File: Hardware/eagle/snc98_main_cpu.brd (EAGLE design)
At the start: 168.1 x 54.1 mm, 151 parts, among them IC1 MCP170333MB, M1 IRLML2244, M10 IRLML2244, M11 IRLML2244, M12 IRLML2244, M2 IRLML2244, M3 IRLML2244, M4 IRLML2244, M5 IRLML2244, M6 IRLML2244, M7 IRLML2244, M8 IRLML2244, M9 IRLML2244, U1 74HC4051_MUX, U3 ATMEGA1284P-PU, U4 TLV70033, X1 MICROMATCH-12, X3 MICROMATCH-12, Y2 12MHz

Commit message: snc98_main_cpu V1.0
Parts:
- removed BH4, BH5: HOLDER_AAA_LEFT1, SparkFun-Electromechanical:BATTERY-AAA-LEFT
- removed BH6: HOLDER_AAA_RIGHT, SparkFun-Electromechanical:BATTERY-AAA-RIGHT
- removed D14, D15, D16, D17, D18, D19, D2, D20, D21, D22, D23, D24, D25, D26, D27: SC40-11_UNISC40-11_UNI, display-hp:10MM_UNI
- removed JP1, JP4: RXD_1, adafruit:1X01-CLEANBIG
- removed JP10, JP11, JP12, JP7, JP8, JP9: (no value), adafruit:1X01
- removed JP2: TXD_1, adafruit:1X01-CLEANBIG
- removed KP1, KP2: KEYPAD, KeyPad3x4:KEYPAD
- removed M10, M11, M4, M5, M6, M7, M8, M9: IRLML2244, IRLML6402:SOT-23
- removed R10, R11, R12, R13, R14, R15, R16, R17, R18, R19, R5, R6, R7, R8, R9: 22, rcl:R1210
- removed R26: 6k8, rcl:0204/5
- removed R29, R54, R55, R56, R57, R58, R59: 3k3, rcl:0204/5
- removed R30: 3V3, rcl:0204/5
- removed R36, R37, R38, R39, R40, R41, R42, R43: 3k3, rcl:R1206
- removed X1, X3: MICROMATCH-12, Con-amp-micromatch:MICROMATCH-12
- added C13: 100n, rcl:C1206K
- added JP15: (no value), adafruit:1X09-BIG
- added JP3: (no value), adafruit:1X08-CLEANBIG
- C1, C2, C3, C6: device _jc:C025_050-025X075 -> _jc:C1206K
- C14, C15, C18, C4, C9: device rcl:C025_050-025X075 -> rcl:C1206K
- C7, C8: device _jc:C025-024X044 -> _jc:C0805K
- LOGO2: value OSHW_LOGO_6MILX0100-NT -> OSHW_LOGO_8MILX0150-NT; device ohw-logo:OSHW_6X100_NOTEXT -> ohw-logo:OSHW_8X150_NOTEXT
- R1, R21, R22, R25, R28, R31, R32, R33, R34, R35, R4, R44, R46, R47, R48, R50, R51: device rcl:0204/7 -> rcl:R1206
- R2: value 6k8 -> 56R
- R20: device rcl:0204/5 -> rcl:R1206
- U$2: device transistor-power:MICRO3 -> transistor-power:SOT-23
- U$3: value HT7333 -> HT7333 / TS9011SCY
- U4: value TLV70033 -> TLV70033 / TC1185
- moved S3 217.4 mm to (152.5, 11.3)
- moved R3 194.3 mm to (138.2, 9.65), flipped to the bottom
- moved R23 179.0 mm to (122.9, 6.60), flipped to the bottom, turned to 270 degrees
- moved D1 171.7 mm to (100.1, 10.2), flipped to the bottom, turned to 90 degrees
- moved U4 170.9 mm to (106.7, 12.2), flipped to the bottom
- moved R25 169.2 mm to (141.2, 7.11), flipped to the bottom, turned to 180 degrees
- moved C5 168.7 mm to (138.2, 12.2), flipped to the bottom
- moved C12 161.6 mm to (126.0, 1.02), flipped to the bottom, turned to 180 degrees
- moved C20 161.1 mm to (90.2, 12.4), flipped to the bottom, turned to 0 degrees
- moved C11 160.7 mm to (109.9, 11.8), flipped to the bottom, turned to 90 degrees
- moved C10 160.4 mm to (125.5, 6.60), flipped to the bottom, turned to 90 degrees
- moved C21 159.1 mm to (95.9, 12.2), flipped to the bottom, turned to 0 degrees
- moved R27 158.2 mm to (120.8, 6.60), flipped to the bottom, turned to 270 degrees
- moved D8 150.1 mm to (80.0, 4.32), flipped to the bottom
- moved U$2 149.4 mm to (117.0, 6.99), flipped to the bottom, turned to 180 degrees
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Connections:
- removed net CA_LED: M10.2, M11.2, M4.2, M5.2, M6.2, M7.2, M8.2, M9.2, R29.1, R30.1, R36.1, R37.1, R38.1, R39.1, R40.1, R41.1, R42.1, R43.1, R54.1, R55.1, R56.1, R57.1, R58.1, R59.1, X3.8
- removed net D0_A: R5.2, X3.1
- removed net D10_A: R15.2, X1.8
- removed net D11_A: R16.2, X1.9
- removed net D12_A: R17.2, X1.10
- removed net D13_A: R18.2, X1.11
- removed net D14_A: R19.2, X1.12
- removed net D1_A: R6.2, X3.2
- removed net D2_A: R7.2, X3.3
- removed net D3_A: R8.2, X3.4
- removed net D4_A: R9.2, X3.5
- removed net D5_A: R10.2, X3.6
- removed net D6_A: R11.2, X3.7
- removed net D7_A: R12.2, X1.5
- removed net D8_A: R13.2, X1.6
- removed net D9_A: R14.2, X1.7
- removed net DIG_0: D2.11, D2.12, D2.13, D2.14, D2.23, D2.28, R5.1
- removed net DIG_1: D14.11, D14.12, D14.13, D14.14, D14.23, D14.28, R6.1
- removed net DIG_10: D23.11, D23.12, D23.13, D23.14, D23.23, D23.28, R15.1
- removed net DIG_11: D24.11, D24.12, D24.13, D24.14, D24.23, D24.28, R16.1
- removed net DIG_12: D25.11, D25.12, D25.13, D25.14, D25.23, D25.28, R17.1
- removed net DIG_13: D26.11, D26.12, D26.13, D26.14, D26.23, D26.28, R18.1
- removed net DIG_14: D27.11, D27.12, D27.13, D27.14, D27.23, D27.28, R19.1
- removed net DIG_2: D15.11, D15.12, D15.13, D15.14, D15.23, D15.28, R7.1
- removed net DIG_3: D16.11, D16.12, D16.13, D16.14, D16.23, D16.28, R8.1
- removed net DIG_4: D17.11, D17.12, D17.13, D17.14, D17.23, D17.28, R9.1
- removed net DIG_5: D18.11, D18.12, D18.13, D18.14, D18.23, D18.28, R10.1
- removed net DIG_6: D19.11, D19.12, D19.13, D19.14, D19.23, D19.28, R11.1
- removed net DIG_7: D20.11, D20.12, D20.13, D20.14, D20.23, D20.28, R12.1
- removed net DIG_8: D21.11, D21.12, D21.13, D21.14, D21.23, D21.28, R13.1
- removed net DIG_9: D22.11, D22.12, D22.13, D22.14, D22.23, D22.28, R14.1
- removed net GND1: C22.2
- removed net IO-A: M4.1, R29.2, R36.2, X1.4
- removed net IO-B: M5.1, R30.2, R37.2, X1.3
- removed net IO-C: M6.1, R42.2, R54.2, X1.2
- removed net IO-D: M7.1, R38.2, R55.2, X1.1
- removed net IO-DP: M11.1, R41.2, R59.2, X3.9
- removed net IO-E: M8.1, R43.2, R56.2, X3.12
- removed net IO-F: M9.1, R39.2, R57.2, X3.11
- removed net IO-G: M10.1, R40.2, R58.2, X3.10
- removed net N$2: U$2.2
- removed net NC1: BH4.P1, BH4.P2, BH4.P3, BH4.P4, BH7.P1, BH7.P2, BH7.P3, BH7.P4
- removed net NC2: BH5.P1, BH5.P2, BH5.P3, BH5.P4
- removed net NC3: BH6.M1, BH6.M2, BH6.M3, BH6.M4
- removed net SEG_A: D14.10, D14.27, D15.10, D15.27, D16.10, D16.27, D17.10, D17.27, D18.10, D18.27, D19.10, D19.27, D2.10, D2.27, D20.10, D20.27, D21.10, D21.27, D22.10, D22.27, D23.10, D23.27, D24.10, D24.27, D25.10, D25.27, D26.10, D26.27, D27.10, D27.27, M4.3
- removed net SEG_B: D14.26, D14.9, D15.26, D15.9, D16.26, D16.9, D17.26, D17.9, D18.26, D18.9, D19.26, D19.9, D2.26, D2.9, D20.26, D20.9, D21.26, D21.9, D22.26, D22.9, D23.26, D23.9, D24.26, D24.9, D25.26, D25.9, D26.26, D26.9, D27.26, D27.9, M5.3
- removed net SEG_C: D14.24, D14.7, D15.24, D15.7, D16.24, D16.7, D17.24, D17.7, D18.24, D18.7, D19.24, D19.7, D2.24, D2.7, D20.24, D20.7, D21.24, D21.7, D22.24, D22.7, D23.24, D23.7, D24.24, D24.7, D25.24, D25.7, D26.24, D26.7, D27.24, D27.7, JP10.1, JP11.1, JP8.1, M6.3
- removed net SEG_D: D14.22, D14.5, D15.22, D15.5, D16.22, D16.5, D17.22, D17.5, D18.22, D18.5, D19.22, D19.5, D2.22, D2.5, D20.22, D20.5, D21.22, D21.5, D22.22, D22.5, D23.22, D23.5, D24.22, D24.5, D25.22, D25.5, D26.22, D26.5, D27.22, D27.5, M7.3
- removed net SEG_DP: D14.25, D14.6, D14.8, D15.25, D15.6, D15.8, D16.25, D16.6, D16.8, D17.25, D17.6, D17.8, D18.25, D18.6, D18.8, D19.25, D19.6, D19.8, D2.25, D2.6, D2.8, D20.25, D20.6, D20.8, D21.25, D21.6, D21.8, D22.25, D22.6, D22.8, D23.25, D23.6, D23.8, D24.25, D24.6, D24.8, D25.25, D25.6, D25.8, D26.25, D26.6, D26.8, D27.25, D27.6, D27.8, JP12.1, JP7.1, JP9.1, M11.3
- removed net SEG_E: D14.21, D14.4, D15.21, D15.4, D16.21, D16.4, D17.21, D17.4, D18.21, D18.4, D19.21, D19.4, D2.21, D2.4, D20.21, D20.4, D21.21, D21.4, D22.21, D22.4, D23.21, D23.4, D24.21, D24.4, D25.21, D25.4, D26.21, D26.4, D27.21, D27.4, M8.3
- removed net SEG_F: D14.2, D14.29, D15.2, D15.29, D16.2, D16.29, D17.2, D17.29, D18.2, D18.29, D19.2, D19.29, D2.2, D2.29, D20.2, D20.29, D21.2, D21.29, D22.2, D22.29, D23.2, D23.29, D24.2, D24.29, D25.2, D25.29, D26.2, D26.29, D27.2, D27.29, M9.3
- removed net SEG_G: D14.1, D14.3, D14.30, D15.1, D15.3, D15.30, D16.1, D16.3, D16.30, D17.1, D17.3, D17.30, D18.1, D18.3, D18.30, D19.1, D19.3, D19.30, D2.1, D2.3, D2.30, D20.1, D20.3, D20.30, D21.1, D21.3, D21.30, D22.1, D22.3, D22.30, D23.1, D23.3, D23.30, D24.1, D24.3, D24.30, D25.1, D25.3, D25.30, D26.1, D26.3, D26.30, D27.1, D27.3, D27.30, M10.3
- net A4: no longer JP4.1
- net A5: now also JP15.8, JP3.8; no longer KP1.C_2, KP2.C_2
- net A6: now also JP15.7, JP3.7; no longer KP1.C_1, KP2.C_1
- net A7: now also JP15.6, JP3.6; no longer KP1.C_0, KP2.C_0
- net A9: no longer R26.2
- net AREF: now also JP15.9
- net D10_: no longer JP1.1
- net D11_: no longer JP2.1
- net EN: no longer R2.2, R26.1
- net GND: now also U$2.2; no longer R2.1, S3.P$15
- net GND-ISO: now also C13.1, JP15.1, JP3.1
- net IO_A: now also JP15.5; no longer KP2.R_0
- net IO_B: now also JP15.4; no longer KP2.R_1
- net IO_C: now also JP15.3; no longer KP2.R_2
- net IO_D: now also JP15.2; no longer KP2.R_3
- net IO_DP: now also JP3.2; no longer KP1.R_3
- net IO_E: now also JP3.5; no longer KP1.R_0
- net IO_F: now also JP3.4; no longer KP1.R_1
- net IO_G: now also JP3.3; no longer KP1.R_2
- net N$1: now also C22.2
- net N$13: now also R2.2
- net N$6: now also R25.2
- net VIN_P: now also R2.1
- net V_IN: now also BH7.P1, BH7.P2, BH7.P3, BH7.P4, C13.2, S3.P$15, U$3.VIN
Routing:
- net SEG_DP: track 347.3 -> 0.00 mm
- net SEG_G: track 337.5 -> 0.00 mm
- net SEG_A: track 335.2 -> 0.00 mm
- net SEG_F: track 306.0 -> 0.00 mm, vias 32 -> 0
- net GND-ISO: track 0.00 -> 303.4 mm, vias 0 -> 15
- net SEG_C: track 281.2 -> 0.00 mm, vias 29 -> 0
- net SEG_B: track 267.0 -> 0.00 mm, vias 15 -> 0
- net V_IN: track 0.00 -> 266.2 mm, vias 0 -> 8
- net SEG_E: track 254.6 -> 0.00 mm, vias 1 -> 0
- net VCC: track 0.00 -> 213.3 mm, vias 0 -> 10
- net SEG_D: track 209.0 -> 0.00 mm, vias 16 -> 0
- net GND: track 0.00 -> 179.5 mm, vias 6 -> 8
- net CA_LED: track 163.1 -> 0.00 mm, vias 4 -> 0
- net N$23: track 0.00 -> 132.4 mm, vias 0 -> 3
- net CA_PWM: track 0.00 -> 108.8 mm, vias 0 -> 3
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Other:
- board size 168.1 x 54.1 mm -> 168.1 x 32.8 mm
- board text added: "CUT OUT"
- board text added: "https://oshpark. com/profiles/Jens_G"
- board text added: "https://oshpark.com/ profiles/Jens_G"
- board text removed: "RESET"
- board text removed: "https://oshpark.com/profiles/Jens_G"

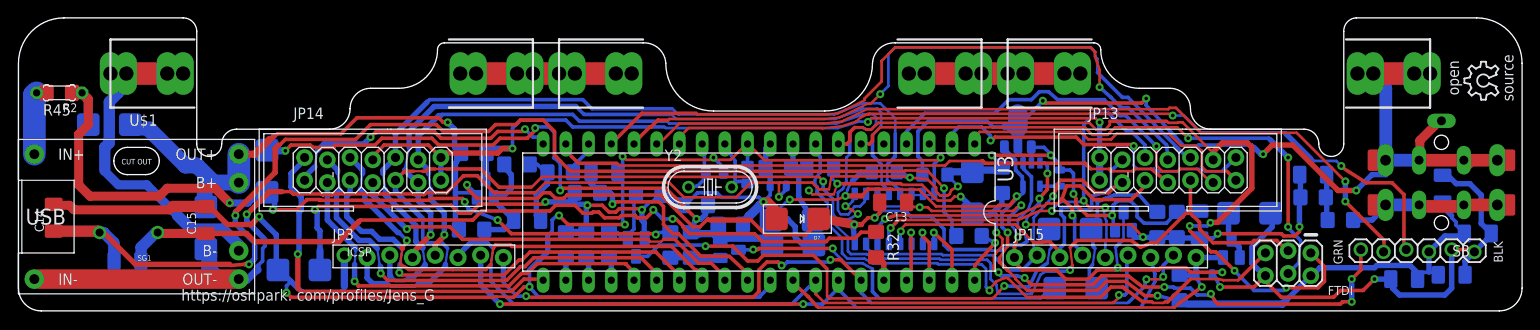
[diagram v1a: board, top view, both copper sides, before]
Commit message: new Reset on Main:cpu
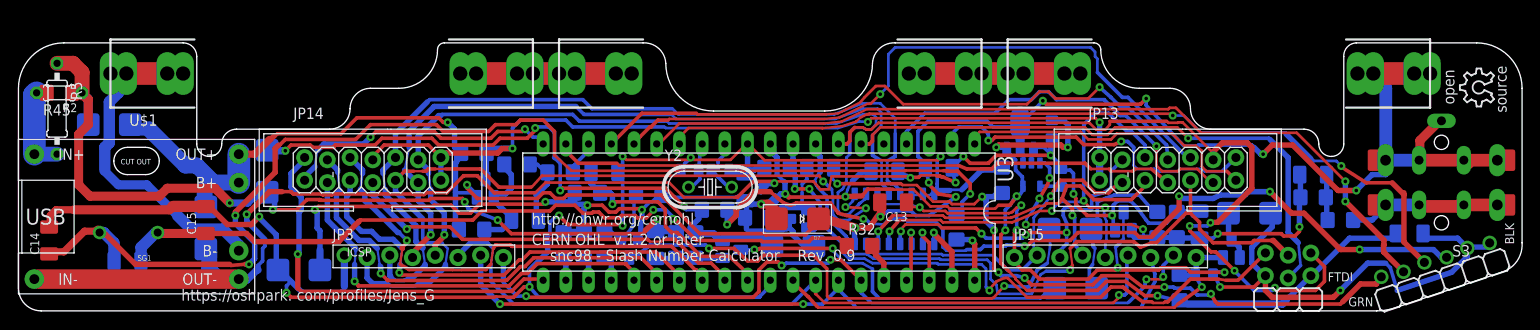
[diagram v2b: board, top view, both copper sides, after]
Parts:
- removed D1, D6: SD103CW, BaseApp:SMADIODE
- removed R24: 2R7, rcl:R1206
- added R5: 56R, rcl:0207/10
- added R6: 22k, rcl:R1206
- added T1: BCR135, digital-transistors:SOT23-BEC
- C3: value 100nF -> 0.1uF; device _jc:C1206K -> SparkFun:0805
- C6: value 10uF -> 15n; device _jc:C1206K -> rcl:C1206K
- R1, R44, R47: value 47k -> 22k
- R20: value 2R7 -> 1k
- R25: value 100 -> 1k
- R31, R32: value 100 -> 150
- R33: value 1k -> 6k8
- SG1: value BUZZERNS -> SBT1205-3
- moved C6 89.1 mm to (64.6, 4.32), turned to 90 degrees
- moved C1 74.4 mm to (74.7, 10.8), turned to 90 degrees
- moved C3 44.2 mm to (109.0, 17.3), turned to 270 degrees
- moved JP6 10.8 mm to (145.8, 0.76), turned to 18.5 degrees
- moved C2 7.62 mm to (149.0, 5.61)
- moved R1 6.04 mm to (76.1, 7.37)
- moved JP5 5.80 mm to (132.8, 0.76), turned to 0 degrees
- moved C7 3.09 mm to (71.9, 12.7), turned to 180 degrees
- moved C8 2.81 mm to (68.5, 12.7), turned to 0 degrees
- moved C14 2.59 mm to (-3.17, 4.83)
- moved R20 2.22 mm to (71.2, 8.26), turned to 180 degrees
- moved R32 1.86 mm to (87.5, 4.22), turned to 0 degrees
- moved R31 1.73 mm to (98.3, 6.35), turned to 90 degrees
- moved C16 1.45 mm to (77.2, 10.0), turned to 45 degrees
- moved LOGO2 0.92 mm to (158.4, 19.8)
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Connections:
- removed net N$12: C18.2, D1.C, JP6.6, R51.2
- new net DTR: C18.2, JP6.1, R51.2
- new net R_: C18.1, R1.2, T1.B
- new net VCC_IN: JP6.4, R20.2
- net /RESET: now also JP5.2, R6.1, T1.E; no longer C18.1, D6.A, JP5.5, R1.2
- net AREF: now also C12.3; no longer C12.1
- net D5_: now also JP5.3; no longer JP5.4
- net D6_: now also JP5.6; no longer JP5.1
- net D7_: now also JP5.4; no longer JP5.3
- net D8_: now also JP6.3; no longer JP6.4
- net D9_: now also JP6.2; no longer JP6.5
- net GND: now also C11.4, C16.4, C3.4; no longer C11.2, C16.2, D1.A, R51.1
- net GND-ISO: now also C12.4, JP5.1, JP6.5, JP6.6, R51.1, R6.2; no longer C12.2, C3.2, C6.2, JP5.6, JP6.1, JP6.2
- net N$13: now also R5.2
- net N$3: now also C11.3; no longer C11.1
- net N$9: now also C6.1
- net VCC: now also C16.3, C3.3, JP5.5, T1.C; no longer C16.1, C3.1, C6.1, D6.C, JP5.2, JP6.3, R20.2, R24.2
- net VIN_P: now also C6.2, R5.1
- net XX_3: no longer R24.1
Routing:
- net VCC_IN: track 0.00 -> 96.0 mm, vias 0 -> 6
- net N$12: track 85.3 -> 0.00 mm, vias 10 -> 0
- net DTR: track 0.00 -> 77.8 mm, vias 0 -> 7
- net V_IN: track 266.2 -> 249.9 mm, vias 8 -> 10
- net R_: track 0.00 -> 9.83 mm
- net VIN_P: track 89.8 -> 97.8 mm
- net GND-ISO: track 303.4 -> 310.3 mm
- net D11_: track 75.8 -> 71.2 mm
- net XX_3: track 77.4 -> 73.5 mm
- net VCC: track 213.3 -> 209.9 mm, vias 10 -> 12
- net N$10: track 90.1 -> 86.9 mm
- net D9_: track 91.5 -> 94.7 mm
- net N$9: track 5.59 -> 8.49 mm
- net D8_: track 92.5 -> 95.1 mm
- net N$13: track 9.24 -> 11.8 mm
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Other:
- board size 168.1 x 32.8 mm -> 168.2 x 30 mm
- board text added: "snc98 - Slash Number Calculator Rev. 0.9"
- board text removed: "snc98 - Slash Number Calculator Rev. 0.8"

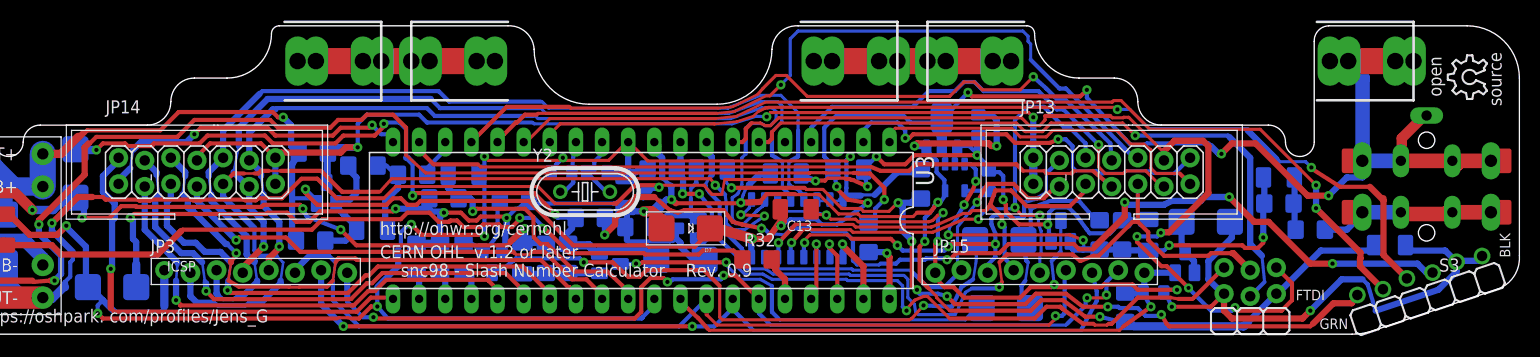
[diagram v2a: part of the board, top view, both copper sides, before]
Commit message: Main_cpu_rev_0.95 - Add Onewire DS18B20
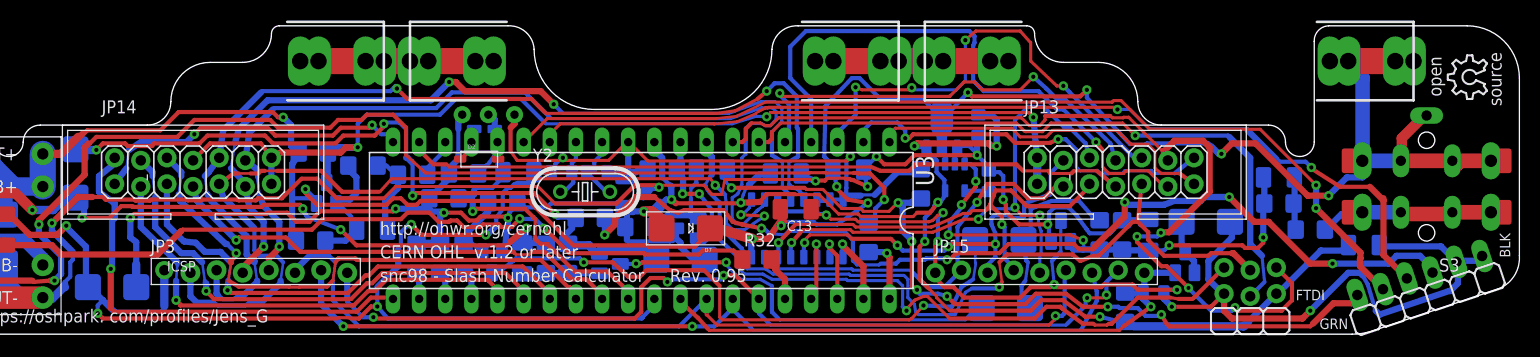
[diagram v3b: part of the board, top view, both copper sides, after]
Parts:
- added D1: SD103CW, BaseApp:SOD-323
- added D2: SD103CW, BaseApp:SOD-123
- added R7: 6k8, rcl:R1206
- added U2: DS18B20, SparkFun-Sensors:TO-92-AMMO
- moved C4 5.34 mm to (64.3, 12.7)
- moved C2 2.54 mm to (146.4, 5.61)
- moved R28 1.15 mm to (62.7, 9.78)
- moved JP13 0.38 mm to (122.3, 12.7)
- moved JP14 0.38 mm to (32.6, 12.7)
- moved BH9 0.25 mm to (108.1, 23.5)
- moved BH10 0.25 mm to (46.9, 23.5)
- moved BH11 0.13 mm to (96.9, 23.5)
- moved BH12 0.13 mm to (58.0, 23.5)
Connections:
- net D8_ renamed D8_RX0
- net D9_ renamed D9_TX0
- removed net D10_: JP13.10, U3.16
- removed net D11_: JP13.8, U3.17
- new net D10_RX1: D1.A, D2.A, R7.1, U2.2, U3.16
- new net D11_TX1: D1.C, D2.C, U3.17
- net D2_: now also JP13.10
- net D4_: now also JP13.8
- net GND-ISO: now also U2.1
- net VCC: now also R7.2, U2.3
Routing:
- net D10_: track 75.5 -> 0.00 mm, vias 1 -> 0
- net D11_: track 71.2 -> 0.00 mm, vias 1 -> 0
- net D2_: track 0.00 -> 45.8 mm, vias 0 -> 4
- net D4_: track 0.00 -> 43.3 mm, vias 0 -> 2
- net D3_: track 43.2 -> 57.5 mm
- net VCC: track 209.9 -> 219.2 mm
- net D10_RX1: track 0.00 -> 8.87 mm
- net GND-ISO: track 310.3 -> 318.6 mm, vias 15 -> 14
- net V_IN: track 249.9 -> 253.6 mm
- net D11_TX1: track 0.00 -> 3.53 mm
- net IO_G: track 93.3 -> 96.2 mm, vias 0 -> 2
- net N$8: track 9.90 -> 7.50 mm
- net AVCC: track 25.7 -> 27.6 mm
- net CA_PWM: track 108.8 -> 110.5 mm
- net N$1: track 14.5 -> 12.8 mm
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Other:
- outline, holes or cut-outs redrawn
- board text added: "snc98 - Slash Number Calculator Rev. 0.95"
- board text removed: "snc98 - Slash Number Calculator Rev. 0.9"

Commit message: fine with 2 numbers
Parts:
- C1: value 100nF -> 220nF
- C12: value 0.1uF -> 47n
- C13, C5: value 100n -> 47n
- C16, C3: value 0.1uF -> 220nF
- C18: value 100n -> 220n
- moved Y2 1.49 mm to (69.3, 10.3)
- moved SG1 1.14 mm to (4.70, 5.21)
- moved C9 1.02 mm to (4.57, 2.54)
- moved R51 0.38 mm to (103.0, 11.6)
- moved D7 0.25 mm to (80.8, 7.24)
- moved R20 0.25 mm to (71.0, 8.26)
- moved R4 0.25 mm to (56.8, 10.2)
- moved D1 0.25 mm to (61.0, 16.6)
- moved R28 0.25 mm to (62.5, 9.78)
- moved R50 0.25 mm to (123.0, -0.43)
- moved C7 0.13 mm to (71.8, 12.7)
- moved C8 0.13 mm to (68.3, 12.7)
- moved U4 0.13 mm to (106.7, 12.1)
- moved M12 0.13 mm to (73.2, 3.68)
- moved C1 0.13 mm to (74.5, 10.8)
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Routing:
- net VIN_P: track 98.0 -> 92.7 mm
- net VCC: track 219.2 -> 224.0 mm
- net D10_RX1: track 8.87 -> 10.9 mm
- net GND-ISO: track 318.6 -> 320.2 mm
- net N$10: track 86.7 -> 87.8 mm
- net XTAL1: track 5.81 -> 6.90 mm
- net GND: track 177.8 -> 178.5 mm
- net N$23: track 133.2 -> 132.6 mm
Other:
- outline, holes or cut-outs redrawn

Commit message: Add new Function: mod (modular)
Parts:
- added T2: BCR135, digital-transistors:SOT23-BEC
- added T3: BCR185, digital-transistors-1(1):SOT23-R_INFINEON
- R2, R45, R5: value 56R -> 150R
- moved T1 3.02 mm to (77.7, 8.00), turned to 180 degrees
- moved C16 2.81 mm to (74.5, 10.9), turned to 0 degrees
- moved C1 2.51 mm to (73.3, 13.0), turned to 0 degrees
- moved C7 2.50 mm to (69.5, 11.7), turned to 90 degrees
- moved R1 1.33 mm to (74.8, 7.75), turned to 90 degrees
- moved S3 0.80 mm to (152.8, 12.1)
- moved IC1 0.74 mm to (106.0, 17.4)
- moved C8 0.74 mm to (67.7, 12.3), turned to 90 degrees
- moved U$3 0.65 mm to (106.0, 16.0)
- moved C11 0.38 mm to (110.4, 11.8)
- moved C3 0.38 mm to (109.3, 17.3)
- moved U4 0.38 mm to (107.1, 12.1)
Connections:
- removed net AREF: C12.3, JP15.9, M1.2, R50.1, U3.32
- new net AREF_+1V: C12.3, JP15.9, M1.2, R50.1, T3.B, U3.32
- new net N$2: T1.E, T3.E
- net /RESET: now also T3.C; no longer T1.E
- net VCC: now also T2.E
- net V_IN: now also T2.B, T2.C
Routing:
- net AREF_+1V: track 0.00 -> 63.8 mm, vias 0 -> 1
- net AREF: track 57.1 -> 0.00 mm, vias 1 -> 0
- net VCC: track 224.0 -> 234.1 mm, vias 12 -> 13
- net V_IN: track 253.7 -> 262.2 mm
- net N$6: track 19.5 -> 24.0 mm
- net XTAL2: track 6.89 -> 9.39 mm
- net N$2: track 0.00 -> 2.13 mm
- net XTAL1: track 6.90 -> 8.75 mm
- net VCC_IN: track 96.7 -> 95.4 mm
- net GND: track 178.5 -> 179.6 mm
- net N$9: track 8.49 -> 7.94 mm
- net /RESET: track 72.7 -> 72.2 mm
- net R_: track 9.83 -> 10.3 mm
- net GND-ISO: track 320.2 -> 319.7 mm, vias 14 -> 15

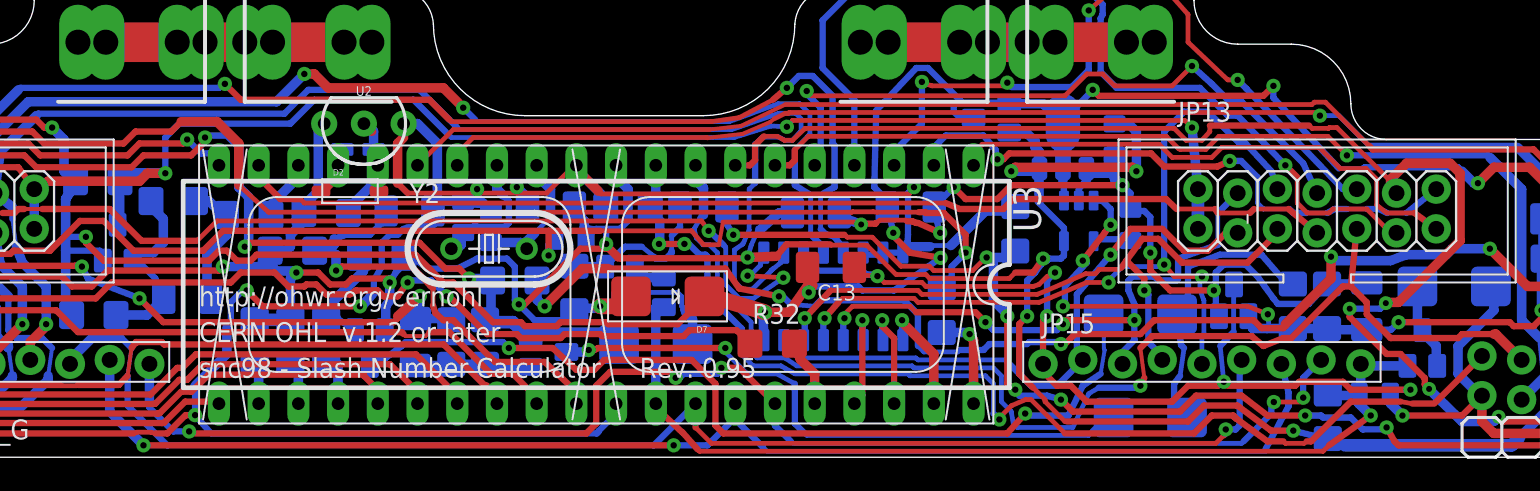
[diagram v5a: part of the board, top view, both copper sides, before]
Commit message: Work like WIN_7 Calculator in "Standard Mode"
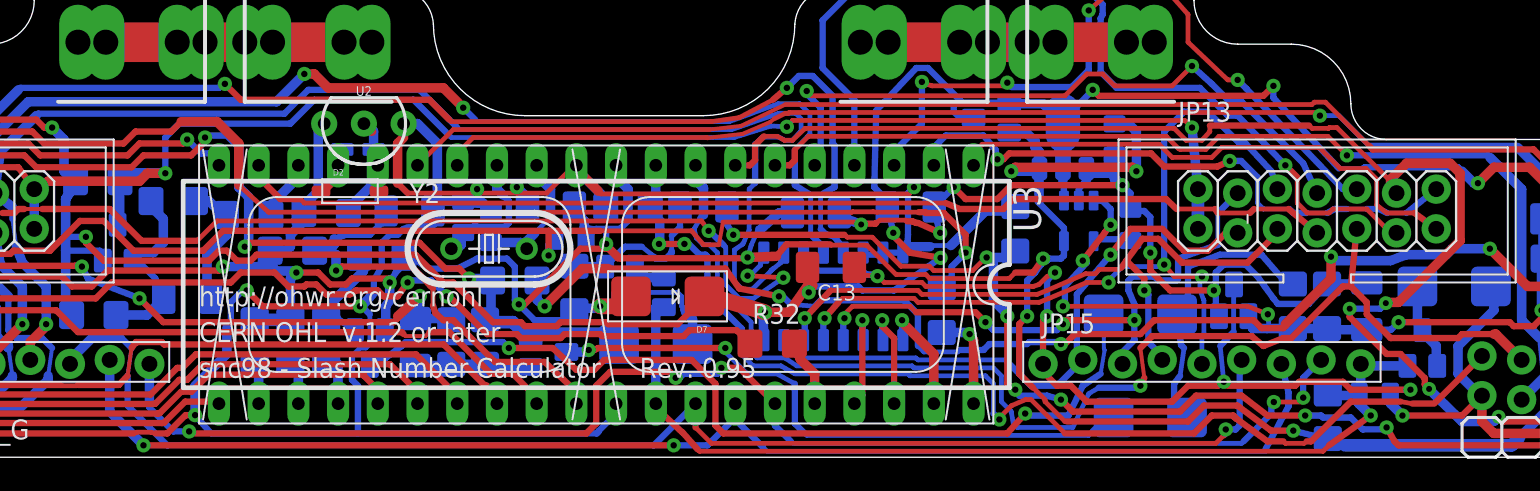
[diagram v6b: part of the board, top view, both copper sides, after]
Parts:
- R1: value 22k -> 47k
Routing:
- net GND-ISO: track 319.7 -> 328.9 mm

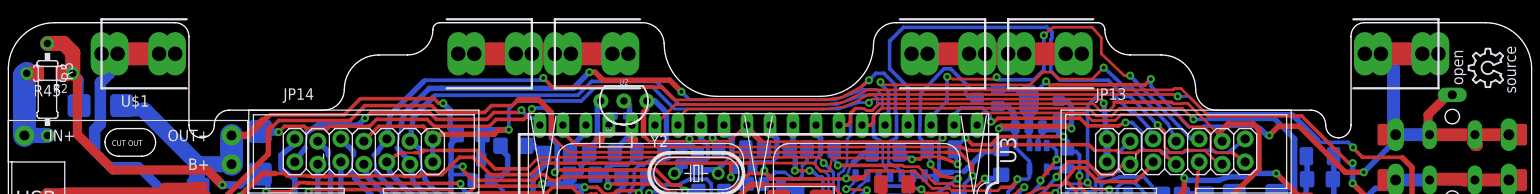
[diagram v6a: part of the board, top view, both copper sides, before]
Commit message: Version 4 mechanical change
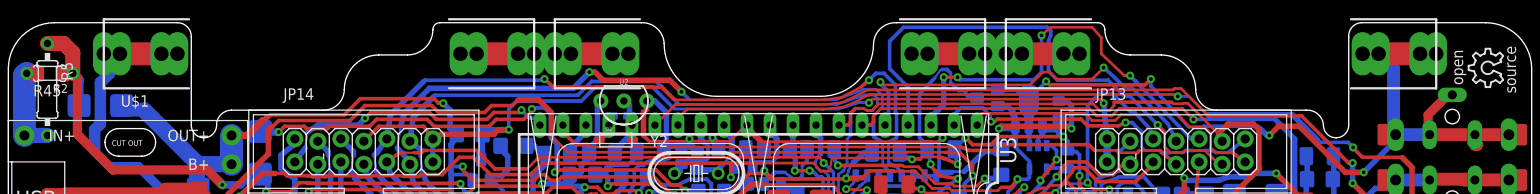
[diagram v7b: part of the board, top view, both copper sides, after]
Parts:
- moved BH9 0.25 mm to (107.8, 23.5)
- moved BH8 0.25 mm to (8.26, 23.5)
- moved BH10 0.25 mm to (47.1, 23.5)
- moved BH7 0.25 mm to (146.7, 23.5)
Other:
- outline, holes or cut-outs redrawn
